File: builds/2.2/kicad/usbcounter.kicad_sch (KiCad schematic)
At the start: 11 parts

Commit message: 2.2: USB interface schematic
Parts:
- added C? (x2): .1u, symbol Device:C
- added D?: TXLED, symbol Device:LED
- added D?: RXLED, symbol Device:LED
- added J?: DISPLAY, symbol Connector:Conn_01x05_Male
- added J?: UJ2-MIBH-G-SMT-TR, UJ2MIBHGSMTTR, symbol Library Loader:UJ2-MIBH-G-SMT-TR
- added R? (x2): R, symbol Device:R
- added R? (x2): 27R, symbol Device:R
- added U?: FT231XS, Package_SO:SSOP-20_3.9x8.7mm_P0.635mm, symbol Interface_USB:FT231XS
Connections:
- net GND: now also C?.1, C?.1, J?.1 (Pin_1), J?.2, U?.16 (GND), U?.6 (GND)
- net VCC: now also D?.2 (A), D?.2 (A), J?.2 (Pin_2), U?.14 (~{RESET}), U?.3 (VCCIO)
- net DISP_CS: now reaches U?.23 (PF3)
- net DISP_CS: now also J?.3 (Pin_3)
- net DISP_DATA: now reaches U?.24 (PF4)
- net DISP_DATA: now also J?.4 (Pin_4)
- net DISP_CLK: now reaches U?.25 (PF5)
- net DISP_CLK: now also J?.5 (Pin_5)
- net PCRX: now reaches U?.30 (XTALHF1/PA0)
- net PCRX: now also U?.4 (RXD)
- net PCTX: now reaches U?.31 (XTALHF2/PA1)
- net PCTX: now also U?.20 (TXD)
- new net: R?.1, U?.10 (CBUS2)
- new net: R?.2, U?.11 (USBDP)
- new net: R?.2, U?.12 (USBDM)
- new net: R?.1, U?.17 (CBUS1)
- new net: D?.1 (K), R?.2 (x2)
- new net: C?.2, J?.3, R?.1
- new net: C?.2, J?.4, R?.1
- new net USB5V: J?.1, U?.15 (VCC)
- no-connect marks 8 -> 19
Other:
- moved on the sheet: C?, J?, R?, SW?, TP?, U?, X?

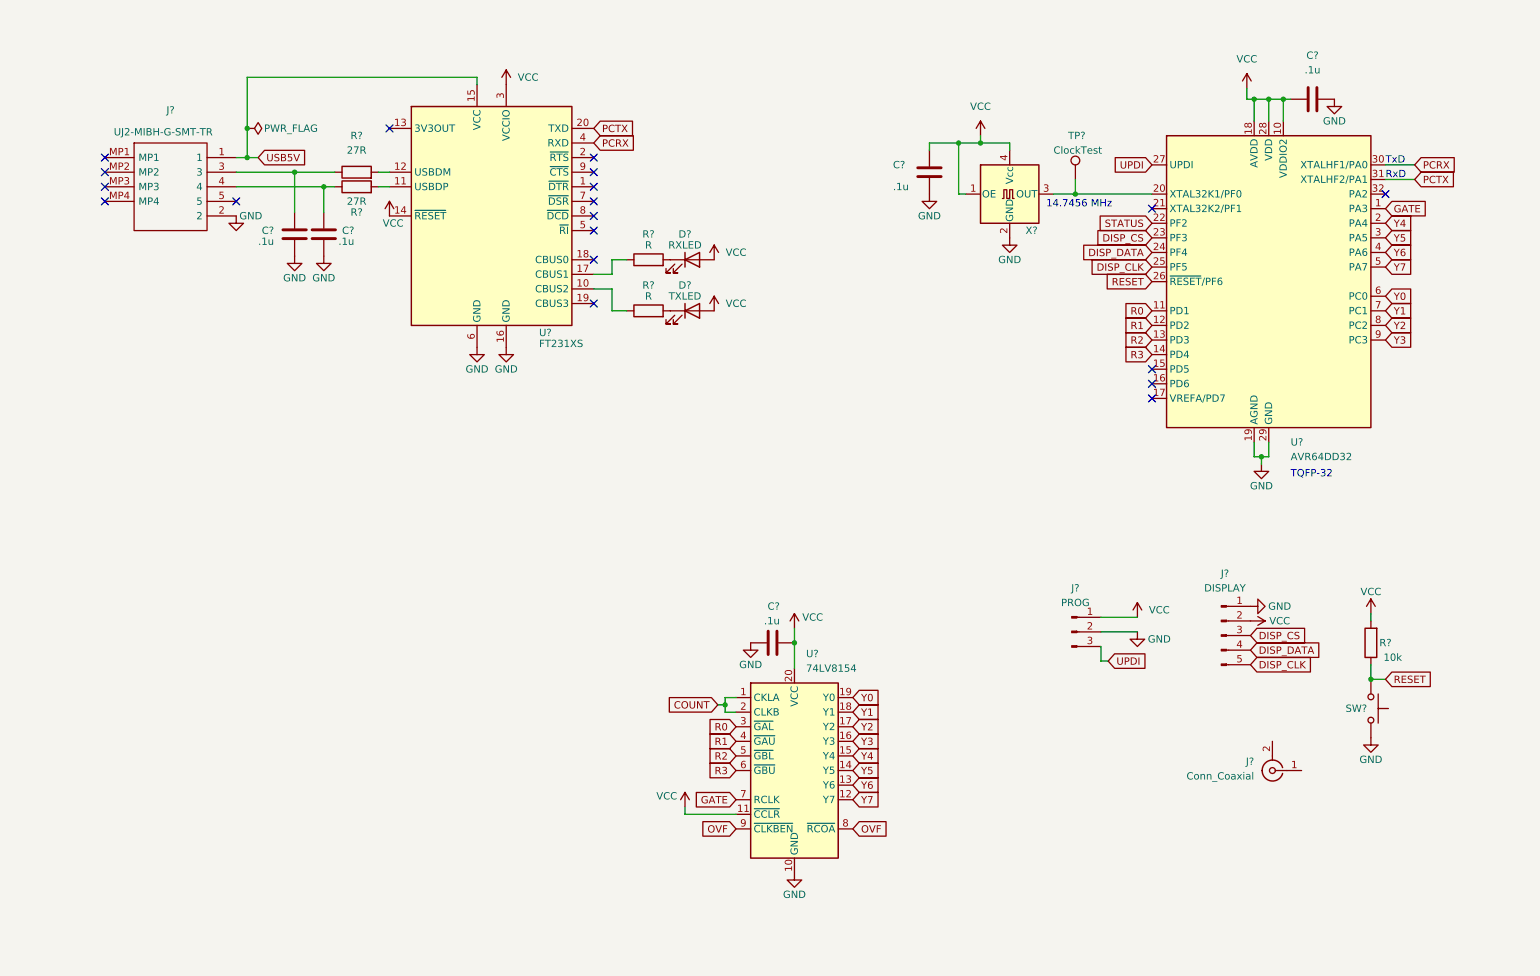
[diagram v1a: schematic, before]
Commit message: 2.2: input signal shaper
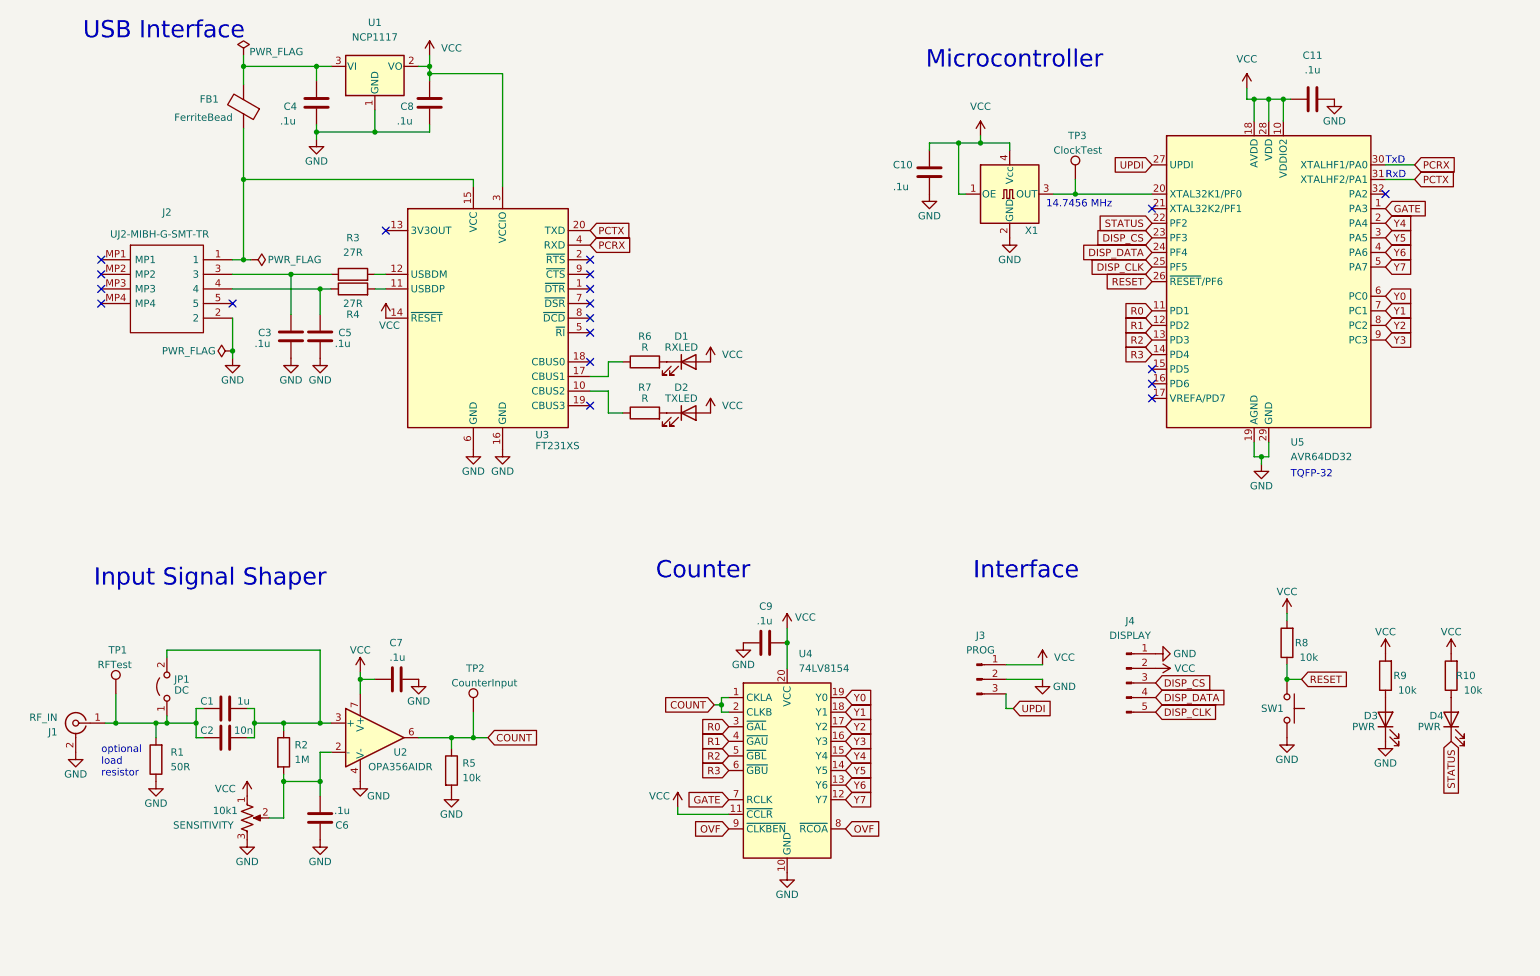
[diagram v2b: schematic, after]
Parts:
- added 10k1: SENSITIVITY, symbol Device:R_Potentiometer_US
- added C1: 1u, symbol Device:C
- added C2: 10n, symbol Device:C
- added C4, C6, C7, C8: .1u, symbol Device:C
- added D3, D4: PWR, symbol Device:LED
- added FB1: FerriteBead, symbol Device:FerriteBead
- added JP1: DC, symbol Jumper:Jumper_2_Open
- added R1: 50R, symbol Device:R
- added R10, R5, R9: 10k, symbol Device:R
- added R2: 1M, symbol Device:R
- added TP1: RFTest, symbol Connector:TestPoint
- added TP2: CounterInput, symbol Connector:TestPoint
- added U1: NCP1117, Package_TO_SOT_SMD:SOT-223-3_TabPin2, symbol Regulator_Linear:NCP1117-3.3_SOT223
- added U2: OPA356AIDR, Package_SO:SOIC-8_3.9x4.9mm_P1.27mm, symbol Amplifier_Operational:OPA356xxD
- J1: renamed from J?; value Conn_Coaxial -> RF_IN
- gave numbers to parts that had none: 21
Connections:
- net COUNT: now also R5.1, TP2.1, U2.6
- net GND: now also J1.2 (Ext), 10k1.3, C4.1, C6.2, C7.1, C8.1, D3.1 (K), R1.1, R5.2, U1.1 (GND), U2.4 (V-)
- net STATUS: now also D4.1 (K)
- net VCC: now also 10k1.1, C7.2, C8.2, R10.2, R9.2, U1.2 (VO), U2.7 (V+)
- net at J1.1 (In): now also C1.1, C2.1, JP1.1 (A), R1.2, TP1.1
- net USB5V: no longer names the net of J2.1, U3.15 (VCC)
- net USB5V: now also FB1.1
- new net: C1.2, C2.2, JP1.2 (B), R2.1, U2.3 (+)
- new net: D3.2 (A), R9.1
- new net: 10k1.2, C6.1, R2.2, U2.2 (-)
- new net: C4.2, FB1.2, U1.3 (VI)
- new net: D4.2 (A), R10.1
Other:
- note added: "Counter"
- note added: "Input Signal Shaper"
- note added: "Interface"
- note added: "Microcontroller"
- note added: "USB Interface"
- note added: "optional load resistor"
- moved on the sheet: C3, C5, C9, D1, D2, J1, J2, J3, J4, R3, R4, R6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

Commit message: 2.2: comparator frontend
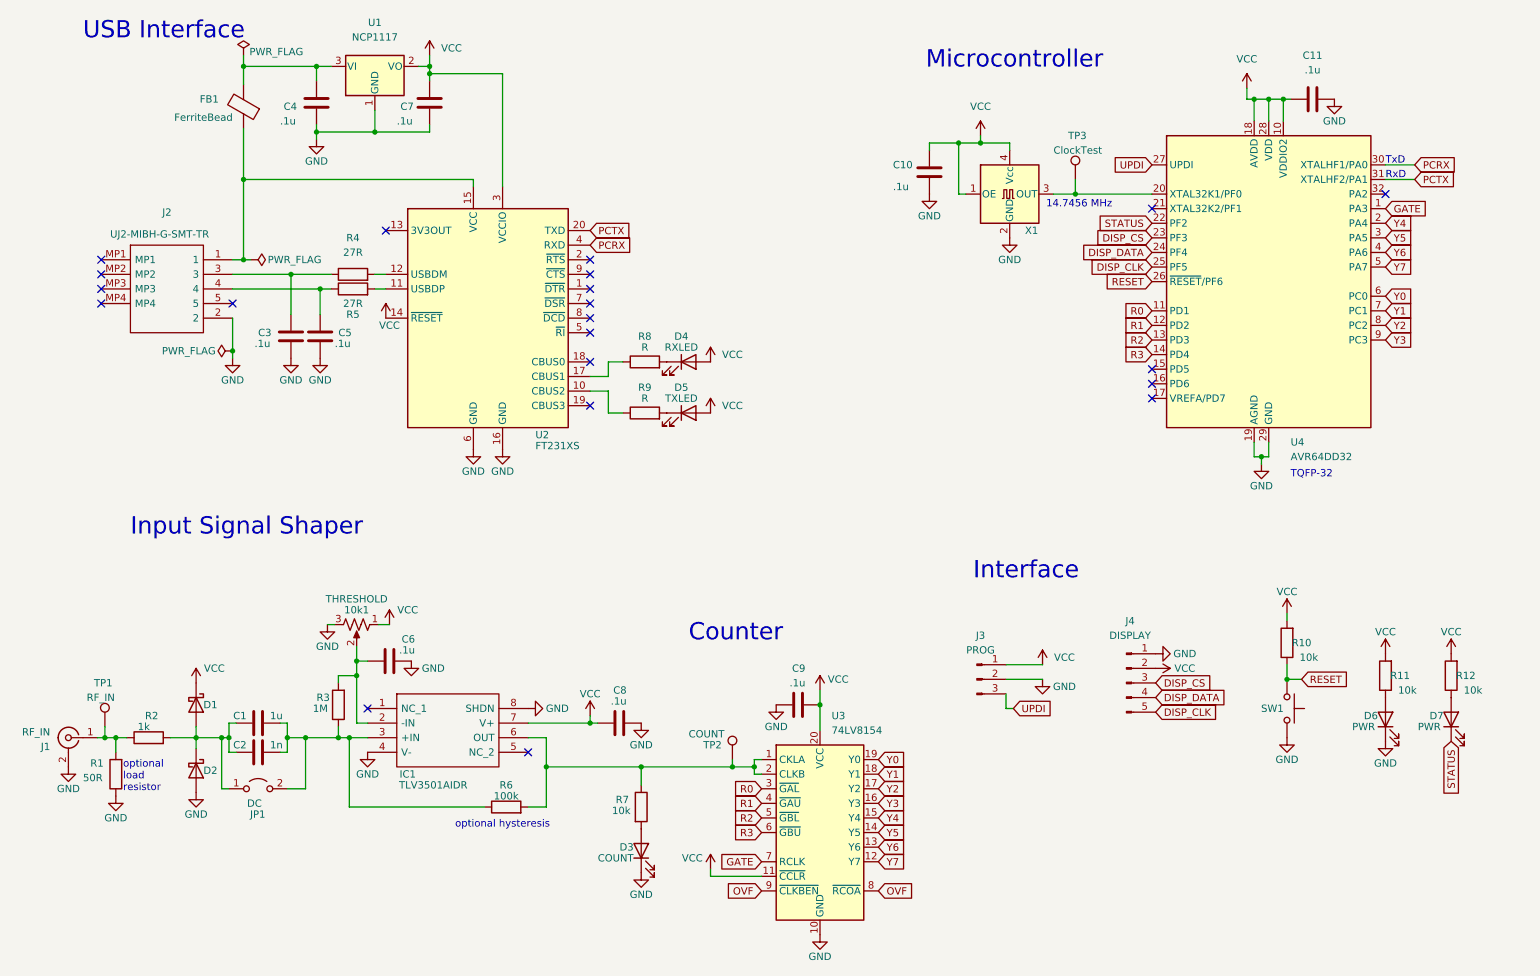
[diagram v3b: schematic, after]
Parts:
- removed C7: .1u, symbol Device:C
- removed U2: OPA356AIDR, Package_SO:SOIC-8_3.9x4.9mm_P1.27mm, symbol Amplifier_Operational:OPA356xxD
- added C8: .1u, symbol Device:C
- added D1, D2: D, symbol Device:D_Schottky
- added D3: COUNT, symbol Device:LED
- added IC1: TLV3501AIDR, SOIC127P600X175-8N, symbol Library Loader:TLV3501AIDR
- added R3: 1M, symbol Device:R
- added R6: 100k, symbol Device:R
- 10k1: value SENSITIVITY -> THRESHOLD
- C2: value 10n -> 1n
- R2: value 1M -> 1k
- TP1: value RFTest -> RF_IN
- TP2: value CounterInput -> COUNT
- renumbered C8 to C7, D1 to D4, D2 to D5, D3 to D6, D4 to D7, R8 to R10, R9 to R11, R10 to R12, R3 to R4, R4 to R5, R5 to R7, R6 to R8, R7 to R9, U3 to U2, U4 to U3, U5 to U4
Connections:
- net GND: now also C8.2, D2.2 (A), D3.1 (K), IC1.4 (V-), IC1.8 (SHDN); no longer R7.2
- net VCC: now also C8.1, D1.1 (K), IC1.7 (V+)
- net at C1.1, C2.1, JP1.1 (A): now also R2.2, D1.2 (A), D2.1 (K); no longer J1.1 (In), R1.2, TP1.1
- net at C1.2, C2.2, JP1.2 (B): now also IC1.3 (+IN), R3.1, R6.1; no longer R2.1
- net at 10k1.2, C6.1: now also IC1.2 (-IN), R3.2; no longer R2.2
- net COUNT: no longer names the net of R7.1, TP2.1, U3.1 (CKLA), U3.2 (CLKB)
- net COUNT: now also IC1.6 (OUT), R6.2
- new net: J1.1 (In), R1.2, R2.1, TP1.1
- new net: D3.2 (A), R7.2
- no-connect marks 19 -> 21
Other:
- note added: "optional hysteresis"
- moved on the sheet: 10k1, C1, C2, C9, J1, JP1, R1, R7, TP1, TP2, U3

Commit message: 2.2: update schematic
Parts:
- removed 10k1: THRESHOLD, symbol Device:R_Potentiometer_US
- removed C6, C8: .1u, symbol Device:C
- removed D3: COUNT, symbol Device:LED
- removed IC1: TLV3501AIDR, SOIC127P600X175-8N, symbol Library Loader:TLV3501AIDR
- removed R10, R7: 10k, symbol Device:R
- removed R3: 1M, symbol Device:R
- removed R6: 100k, symbol Device:R
- removed SW1: SW_MEC_5G, symbol Switch:SW_MEC_5G
- removed TP3: ClockTest, symbol Connector:TestPoint
- added D?: COUNT, symbol Device:LED
- added JP?: GATE, symbol Jumper:SolderJumper_2_Bridged
- added R? (x2): 10k, symbol Device:R
- added R? (x2): 100k, symbol Device:R
- added SW?: RESET, symbol Switch:SW_MEC_5G
- added TP?: GATE, symbol Connector:TestPoint
- added TP?: CKOUT, symbol Connector:TestPoint
- added U?: 74LVC1G14, Package_TO_SOT_SMD:SOT-23-5, symbol 74xGxx:SN74LVC1G14DBV
- D7: value PWR -> STATUS
- R8, R9: value R -> 10k
- U4: value AVR64DD32 -> AVR64DD32 TQFP32
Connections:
- net GATE: now also U4.4 (PA6), JP?.2 (B); no longer U3.7 (RCLK), U4.1 (PA3)
- net GND: now also C10.2, C11.1, D?.1 (K), R?.1, SW?.3 (B), SW?.4 (B), U?.3 (GND); no longer C10.1, C11.2
- net RESET: now also R?.2, SW?.1 (A), SW?.2 (A)
- net VCC: now also C10.1, C11.2, R?.1, R?.2, U?.5 (VCC); no longer C10.2, C11.1
- net Y4: now also U4.32 (PA2); no longer U4.2 (PA4)
- net Y5: now also U4.1 (PA3); no longer U4.3 (PA5)
- net Y6: now also U4.2 (PA4); no longer U4.4 (PA6)
- net Y7: now also U4.3 (PA5); no longer U4.5 (PA7)
- net at C1.2, C2.2, JP1.2 (B): now also R?.1, R?.2, U?.2
- net at TP2.1, U3.1 (CKLA), U3.2 (CLKB): now also R?.2, U?.4
- net at U4.17 (VREFA/PD7): now also D7.1 (K)
- net STATUS: no longer names the net of U4.22 (PF2)
- net STATUS: no longer D7.1 (K)
- new net: D?.2 (A), R?.1
- new net: JP?.1 (A), TP?.1, U3.7 (RCLK)
- new net: TP?.1, U4.5 (PA7)
- no-connect marks 21 -> 17
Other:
- note added: "10 MHz"
- note removed: "14.7456 MHz"
- note removed: "Input Signal Shaper"
- note removed: "Interface"
- note removed: "TQFP-32"
- note removed: "optional hysteresis"
- company: (none) -> Harden Technologies, LLC
- title: (none) -> USB Counter
- moved on the sheet: C1, C10, C11, C2, C3, C4, C5, C7, C9, D1, D2, D4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

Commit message: 2.2: update schematic
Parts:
- added H1, H2, H3, H4: MountingHole, symbol Mechanical:MountingHole
- gave numbers to parts that had none: 10
- renumbered C3 to C1, C4 to C2, C5 to C3, C1 to C4, C2 to C5, C7 to C6, C9 to C7, C10 to C8, C11 to C9, D6 to D4, D4 to D5, D5 to D6, J2 to J1, J1 to J2, R9 to R10, R12 to R11, R4 to R3, R5 to R4, R11 to R7, R8 to R9, U2 to U3, U3 to U4, U4 to U5
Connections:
- net at U5.16 (PD6): now also D7.1 (K)
- net at U5.17 (VREFA/PD7): no longer D7.1 (K)
- no-connect marks 17 -> 18
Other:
- moved on the sheet: D7, R11

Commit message: 2.2: update footprints
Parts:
- C1, C2, C3, C4, C5, C6, C7, C8, C9: footprint (none) -> Capacitor_SMD:C_0805_2012Metric_Pad1.18x1.45mm_HandSolder
- D1, D2, D3, D4, D5, D6, D7: footprint (none) -> LED_SMD:LED_0805_2012Metric_Pad1.15x1.40mm_HandSolder
- FB1: footprint (none) -> Inductor_SMD:L_0805_2012Metric_Pad1.15x1.40mm_HandSolder
- H1, H2, H3, H4: footprint (none) -> MountingHole:MountingHole_4.3mm_M4_Pad
- J1: footprint UJ2MIBHGSMTTR -> Library Loader:UJ2MIBHGSMTTR
- J2: footprint (none) -> Connector_Coaxial:SMA_Amphenol_901-144_Vertical
- J3: footprint (none) -> Connector_PinHeader_2.54mm:PinHeader_1x03_P2.54mm_Vertical
- J4: footprint (none) -> Connector_PinHeader_2.54mm:PinHeader_1x04_P2.54mm_Vertical
- JP1: footprint (none) -> Jumper:SolderJumper-2_P1.3mm_Open_RoundedPad1.0x1.5mm
- JP2: footprint (none) -> Jumper:SolderJumper-2_P1.3mm_Bridged_RoundedPad1.0x1.5mm
- R1: footprint (none) -> Resistor_THT:R_Axial_DIN0207_L6.3mm_D2.5mm_P7.62mm_Horizontal
- R10, R11, R12, R2, R3, R4, R5, R6, R7, R8, R9: footprint (none) -> Resistor_SMD:R_0805_2012Metric_Pad1.20x1.40mm_HandSolder
- SW1: footprint (none) -> Button_Switch_SMD:SW_SPST_TL3342
- TP1, TP2, TP3, TP4: footprint (none) -> TestPoint:TestPoint_Pad_D2.0mm
- U4: footprint (none) -> Package_SO:TSSOP-20_4.4x6.5mm_P0.65mm
